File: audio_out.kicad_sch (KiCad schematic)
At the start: 1 part, among them J1 PJ-611C

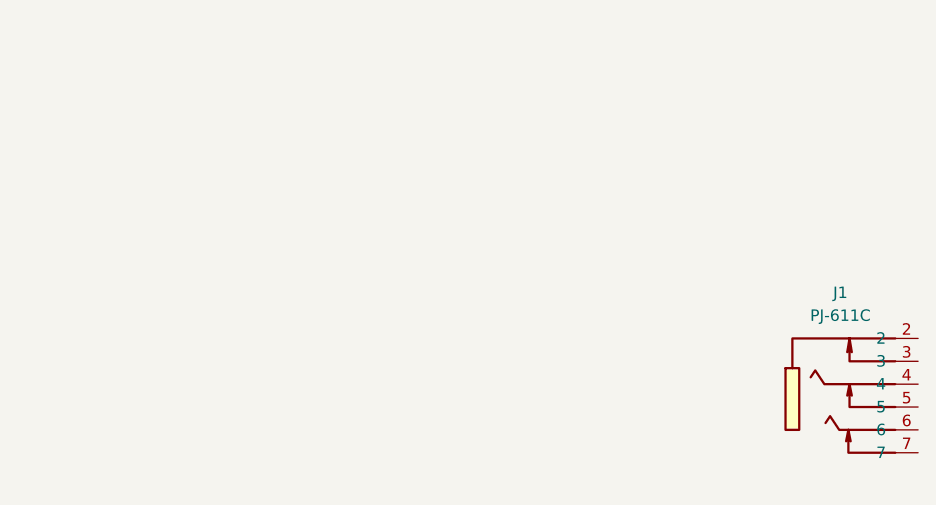
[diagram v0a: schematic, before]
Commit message: Initial design of CS43131 and level shifters
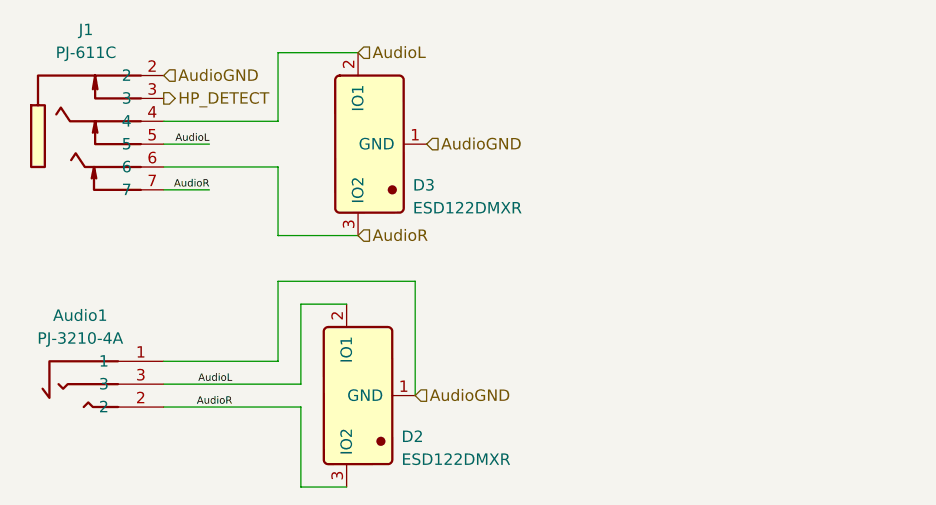
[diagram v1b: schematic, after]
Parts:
- added Audio1: PJ-3210-4A, JLCImport:PJ-3210-4A, symbol JLCImport:PJ-3210-4A
- added D2, D3: ESD122DMXR, JLCImport:ESD122DMXR, symbol JLCImport:ESD122DMXR
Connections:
- net AudioGND: now reaches J1.2
- net AudioGND: now also Audio1.1, D2.1 (GND), D3.1 (GND)
- net HP_DETECT: now reaches J1.3
- net AudioL: now reaches J1.4
- net AudioL: now also J1.5, Audio1.3, D2.2 (IO1), D3.2 (IO1)
- net AudioR: now reaches J1.6
- net AudioR: now also J1.7, Audio1.2, D2.3 (IO2), D3.3 (IO2)
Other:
- moved on the sheet: J1
